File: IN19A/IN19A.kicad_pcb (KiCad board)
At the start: 2 copper layers, 18 x 18 mm, 16 parts

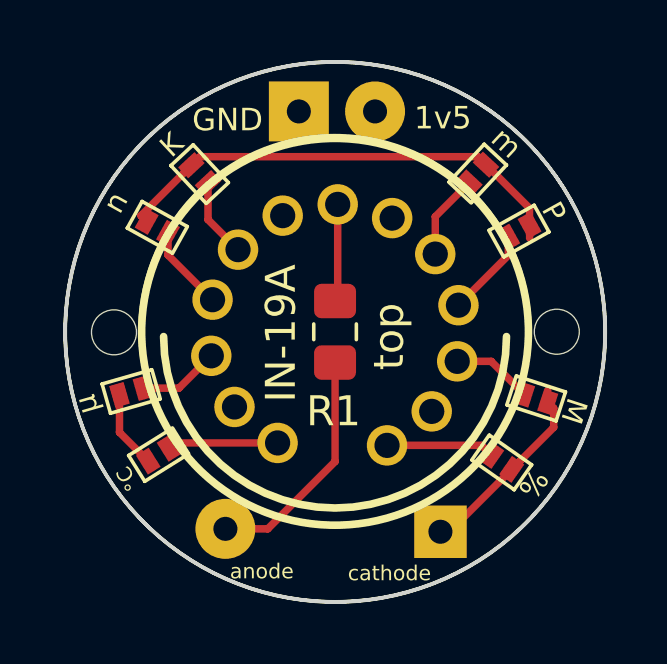
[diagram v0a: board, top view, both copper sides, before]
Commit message: Add files via upload
15 NOV 2020 11:06 PM changed trace width from .25mm to .4 - .75mm.
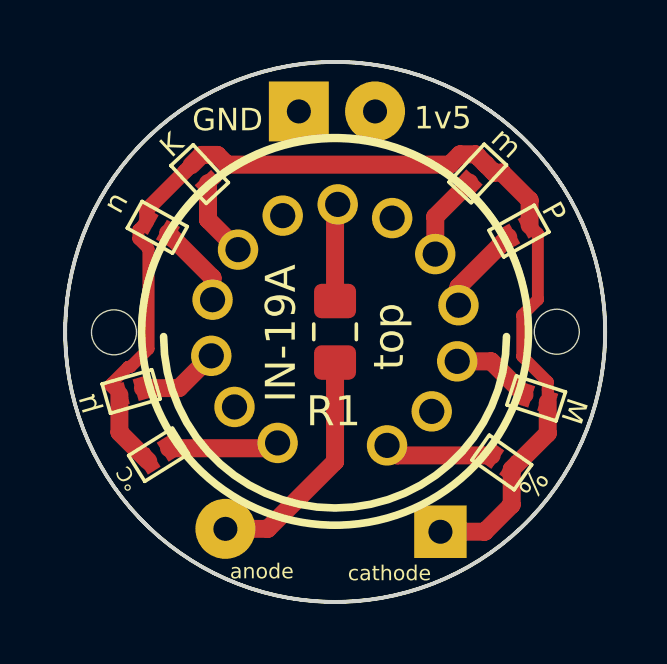
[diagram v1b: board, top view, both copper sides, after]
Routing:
- net Net-(J2-Pad1): track 24.9 -> 38.2 mm
